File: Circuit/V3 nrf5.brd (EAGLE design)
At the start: 41 x 64.5 mm, 58 parts, among them J4 USB Micro, J7 CORTEX_DEBUG_SMD, Q1 FDV301N, Q2 BSS84, Q3 FDV301N, U2 MCP73831, U3 BC840M, U4 MIC5205, U8 TPS61236P, Y1 32.768kHz

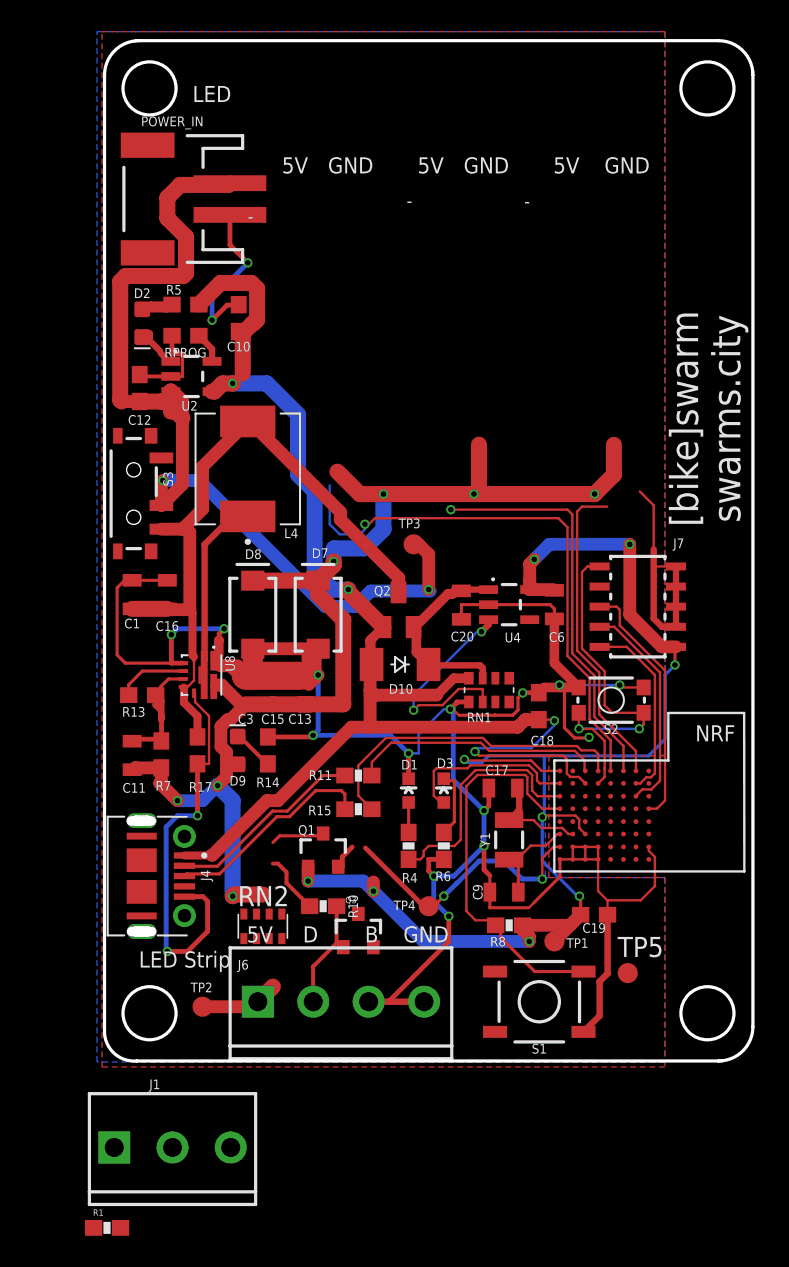
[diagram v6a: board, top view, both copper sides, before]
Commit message: Finishing V7 of the board. All connectors are on two sides of the board now, making the enclosure more seamless. Off to the board house!
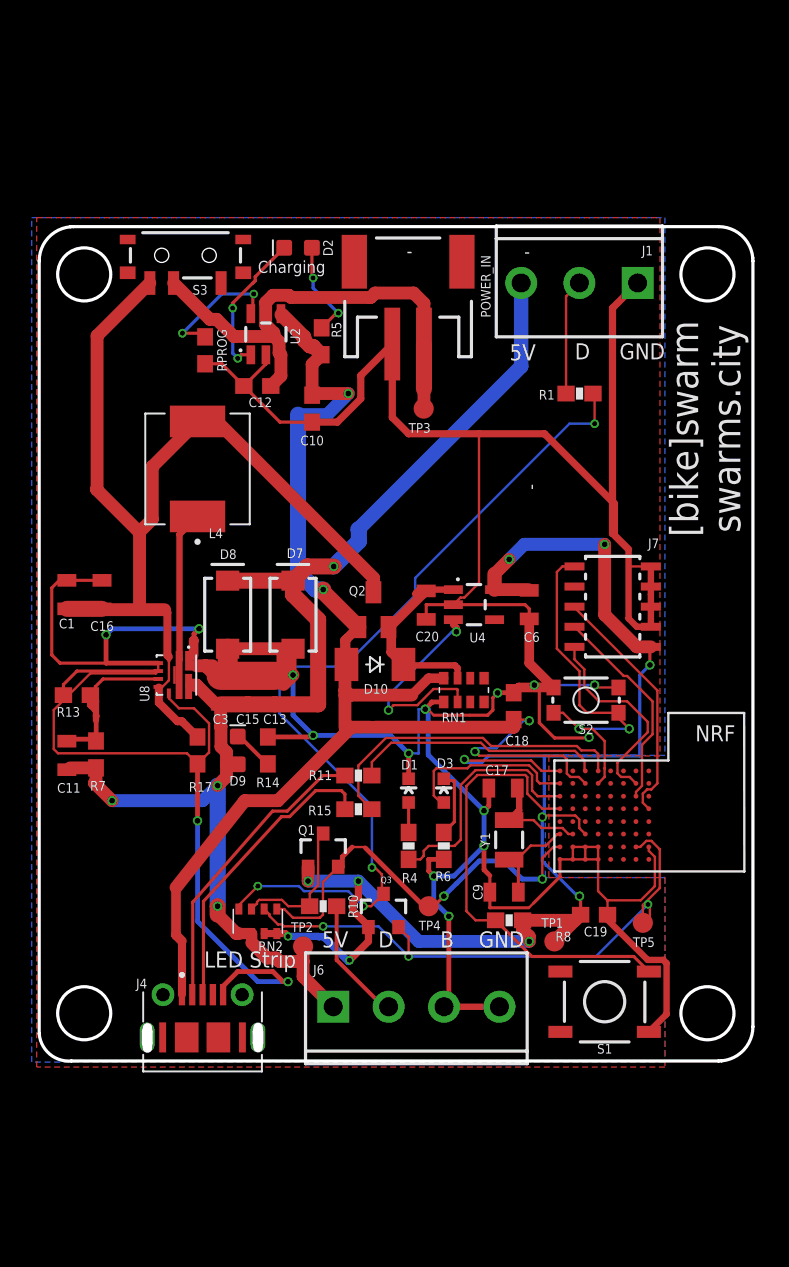
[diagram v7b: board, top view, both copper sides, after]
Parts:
- moved J1 63.7 mm to (33.7, 49.5), turned to 180 degrees
- moved R1 60.6 mm to (30.2, 42.5)
- moved POWER_IN 15.9 mm to (19.3, 49.4), turned to 0 degrees
- moved S3 15.4 mm to (5.27, 51.3), turned to 0 degrees
- moved D2 10.9 mm to (12.4, 51.8), turned to 180 degrees
- moved J4 10.4 mm to (6.35, 2.22), turned to 0 degrees
- moved R5 8.91 mm to (13.9, 45.8), turned to 270 degrees
- moved TP3 8.60 mm to (20.3, 41.6)
- moved C12 7.43 mm to (9.81, 43.0), turned to 180 degrees
- moved TP2 7.41 mm to (12.7, 7.62)
- moved C10 7.36 mm to (13.3, 41.6), turned to 270 degrees
- moved U2 5.40 mm to (10.4, 46.3), turned to 0 degrees
- moved J6 4.77 mm to (14.6, 3.81)
- moved S1 4.13 mm to (31.8, 4.13)
- moved C1 4.13 mm to (-2.22, 29.8)
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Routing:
- net GND: track 229.3 -> 314.8 mm, vias 18 -> 16
- net HEADLAMP_5V: track 0.00 -> 56.5 mm, vias 0 -> 4
- net HEADLAMP_3V3: track 0.00 -> 37.4 mm, vias 0 -> 3
- net CTRL_CH1: track 35.1 -> 0.00 mm, vias 1 -> 0
- net VBAT_S: track 65.0 -> 31.0 mm, vias 2 -> 0
- net CTRL_CH2: track 25.4 -> 0.00 mm, vias 1 -> 0
- net VBAT: track 43.9 -> 64.8 mm
- net CTRL_CH3: track 19.9 -> 0.00 mm
- net 3.3V: track 83.9 -> 95.0 mm, vias 9 -> 11
- net STRIP_3V3: track 18.9 -> 26.4 mm
- net N$17: track 0.00 -> 7.33 mm
- net N$12: track 12.5 -> 19.0 mm
- net N$14: track 2.96 -> 9.39 mm, vias 0 -> 2
- net N$11: track 1.97 -> 8.38 mm, vias 0 -> 2
- net N$16: track 13.4 -> 18.9 mm
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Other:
- board size 41 x 64.5 mm -> 45.1 x 52.7 mm
- board text added: "Charging"
- board text added: "[bike]swarm V7 3/12/2021 swarms.city"
- board text removed: "LED"
- board text removed: "[bike]swarm V6 1/19/2021 swarms.city"

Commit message: Updating with in stock digikey components. Subbing adjustable boost converter for fixed.
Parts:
- removed R13: 100k, SparkFun-Resistors:0603
- removed R7: 1M, SparkFun-Resistors:0603@1
- U8: value TPS61236P -> TPS61235P
- moved C11 4.77 mm to (2.54, 19.4)
- moved C1 1.59 mm to (-0.64, 29.8)
- moved C16 1.59 mm to (1.59, 29.8)
- moved C9 0.19 mm to (25.4, 11.2)
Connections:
- removed net N$9: C11.2, R13.2, R7.1, U8.6
- net 5V: now also U8.6; no longer R7.2
- net GND: now also C11.2; no longer R13.1
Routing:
- net GND: track 314.8 -> 297.6 mm
- net N$9: track 13.4 -> 0.00 mm
- net 5V: track 84.9 -> 90.2 mm, vias 4 -> 5
- net VBAT: track 64.8 -> 63.8 mm
